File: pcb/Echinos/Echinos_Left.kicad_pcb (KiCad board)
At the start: 2 copper layers, 167.4 x 138.9 mm, 134 parts, among them J200 USB_B_Micro, J201 Conn_01x04_Socket, J202 Conn_01x12_Socket, J203 Conn_01x06_Socket, J204 Conn_01x06_Socket, J205 Conn_01x06_Socket, J206 USB_C_Receptacle_USB2.0, J207 Conn_01x05_Socket, SW200 SW_Push, SW201 SW_Push, SW202 SW_Push, SW203 SW_Push, SW204 SW_Push, SW205 SW_Push, SW206 SW_Push, SW207 SW_Push, SW208 SW_Push, SW209 SW_Push, SW210 SW_Push, SW211 SW_Push, SW212 SW_Push, SW213 SW_Push, SW214 SW_Push, SW215 SW_Push, SW216 SW_Push, SW217 SW_Push, SW218 SW_Push, SW219 SW_Push, SW220 SW_Push, SW221 SW_Push, SW222 SW_Push, SW223 SW_Push, SW224 Button, SW225 Button, SW226 Button, SW227 Button, U200 W25Q128JVP, U201 RP2040, U202 USBLC6-2P6, U203 74LVC1T45, U204 USBLC6-2P6, U205 XC6210B332MR-G, Y200 Crystal_GND24

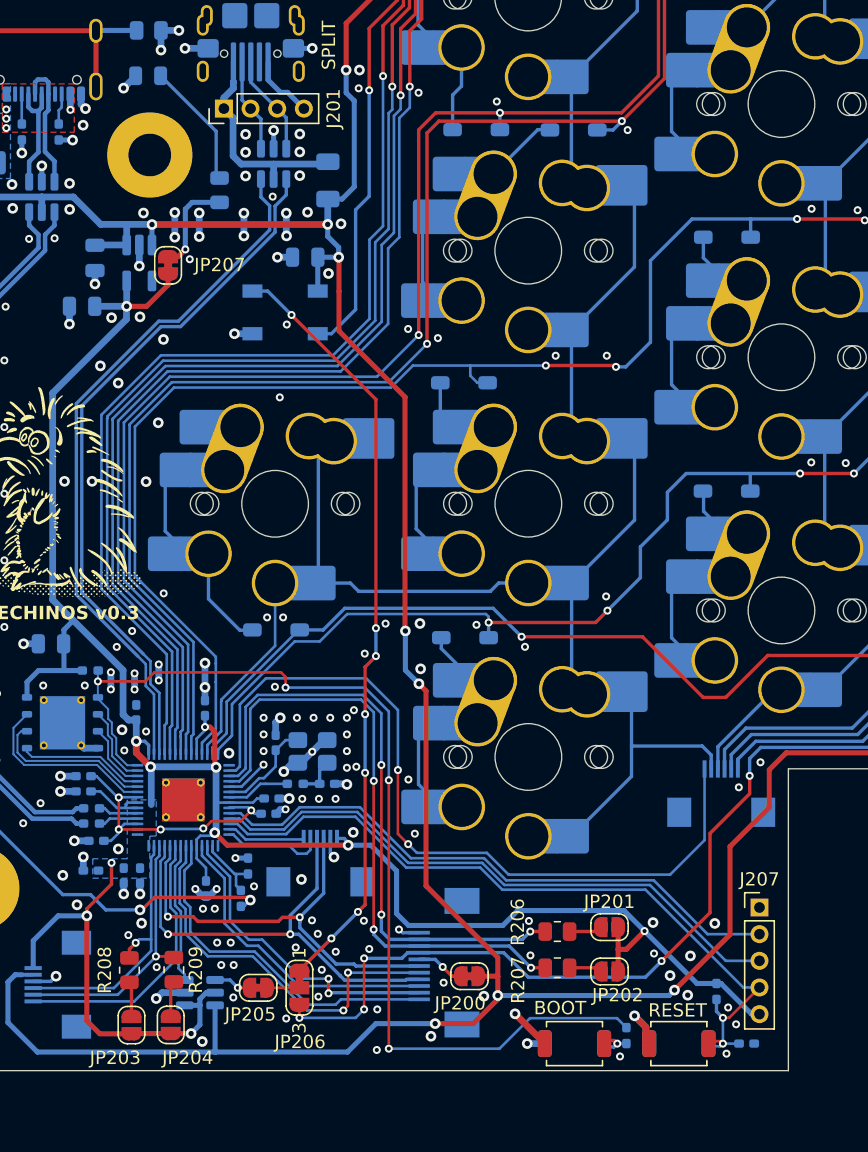
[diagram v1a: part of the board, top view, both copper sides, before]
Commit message: 💥 [PCB] - Split schematic for left and right halves.   - Required to create a common PCB to lower the manufacturing cost
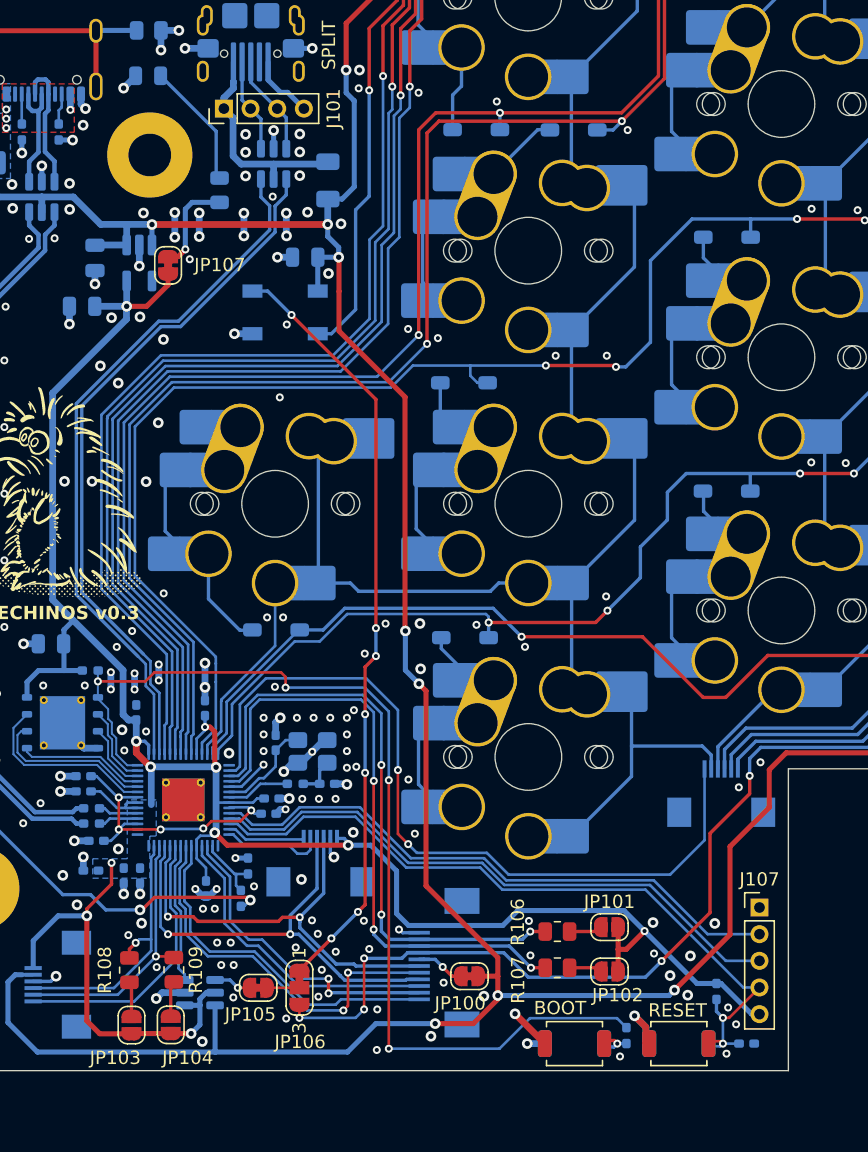
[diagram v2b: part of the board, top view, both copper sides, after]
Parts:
- renumbered C200 to C100, C201 to C101, C202 to C102, C203 to C103, C204 to C104, C205 to C105, C206 to C106, C207 to C107, C208 to C108, C209 to C109, C210 to C110, C211 to C111, C212 to C112, C213 to C113, C214 to C114, C215 to C115, C216 to C116, C217 to C117, C218 to C118, C219 to C119, C220 to C120, C221 to C121, C222 to C122, C223 to C123, C224 to C124, D200 to D100, D201 to D101, D202 to D102, D203 to D103, D204 to D104, D205 to D105, D206 to D106, D207 to D107, D208 to D108, D209 to D109, D210 to D110, D211 to D111, D212 to D112, D213 to D113, D214 to D114, D215 to D115, D216 to D116, D217 to D117, D218 to D118, D219 to D119, D220 to D120, D221 to D121, D222 to D122, D223 to D123, D224 to D124, D225 to D125, D226 to D126, D227 to D127, D228 to D128, D229 to D129, D230 to D130, D231 to D131, D232 to D132, F200 to F100, F201 to F101, FB200 to FB100, H200 to H100, H201 to H101, H202 to H102, H203 to H103, H204 to H104, H205 to H105, J200 to J100, J201 to J101, J202 to J102, J203 to J103, J204 to J104, J205 to J105, J206 to J106, J207 to J107, JP200 to JP100, JP201 to JP101, JP202 to JP102, JP203 to JP103, JP204 to JP104, JP205 to JP105, JP206 to JP106, JP207 to JP107, R200 to R100, R201 to R101, R202 to R102, R203 to R103, R204 to R104, R205 to R105, R206 to R106, R207 to R107, R208 to R108, R209 to R109, R210 to R110, R211 to R111, R212 to R112, R213 to R113, R214 to R114, SW200 to SW100, SW201 to SW101, SW202 to SW102, SW203 to SW103, SW204 to SW104, SW205 to SW105, SW206 to SW106, SW207 to SW107, SW208 to SW108, SW209 to SW109, SW210 to SW110, SW211 to SW111, SW212 to SW112, SW213 to SW113, SW214 to SW114, SW215 to SW115, SW216 to SW116, SW217 to SW117, SW218 to SW118, SW219 to SW119, SW220 to SW120, SW221 to SW121, SW222 to SW122, SW223 to SW123, SW224 to SW124, SW225 to SW125, SW226 to SW126, SW227 to SW127, U200 to U100, U201 to U101, U202 to U102, U203 to U103, U204 to U104, U205 to U105, Y200 to Y100
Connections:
- net /Split/Backlight/backlight_in renamed /Left/Backlight/backlight_in
- net /Split/P_USB+ renamed /Left/P_USB+
- net /Split/P_USB- renamed /Left/P_USB-
- net /Split/RP2040/GPIO12 renamed /Left/RP2040/GPIO12
- net /Split/RP2040/GPIO18 renamed /Left/RP2040/GPIO18
- net /Split/RP2040/GPIO19 renamed /Left/RP2040/GPIO19
- net /Split/RP2040/QSPI_SCLK renamed /Left/RP2040/QSPI_SCLK
- net /Split/RP2040/QSPI_SD0 renamed /Left/RP2040/QSPI_SD0
- net /Split/RP2040/QSPI_SD1 renamed /Left/RP2040/QSPI_SD1
- net /Split/RP2040/QSPI_SD2 renamed /Left/RP2040/QSPI_SD2
- net /Split/RP2040/QSPI_SD3 renamed /Left/RP2040/QSPI_SD3
- net /Split/RP2040/QSPI_SS renamed /Left/RP2040/QSPI_SS
- net /Split/USB+ renamed /Left/USB+
- net /Split/USB- renamed /Left/USB-
